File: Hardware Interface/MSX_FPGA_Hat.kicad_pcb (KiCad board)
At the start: 2 copper layers, 103 x 66 mm, 26 parts, among them J1 J1, J2 J2, J3a1 J3a, J3b1 J3b, J4a1 J4a, J4b1 J4b, U1 74LVC245A, U2 74LVC245A, U3 74LVC245A, U4 74LVC245A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

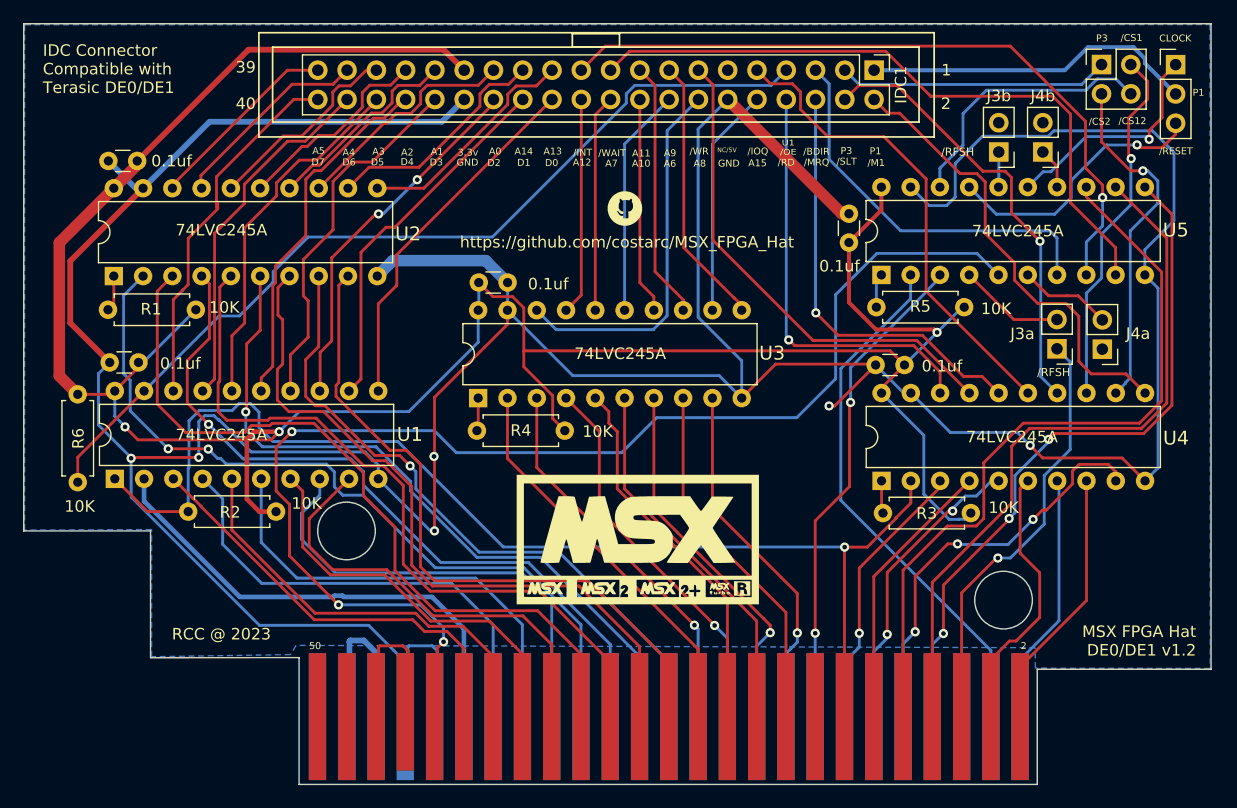
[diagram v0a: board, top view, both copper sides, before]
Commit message: Updated Add-On with silk in addresses for RPI
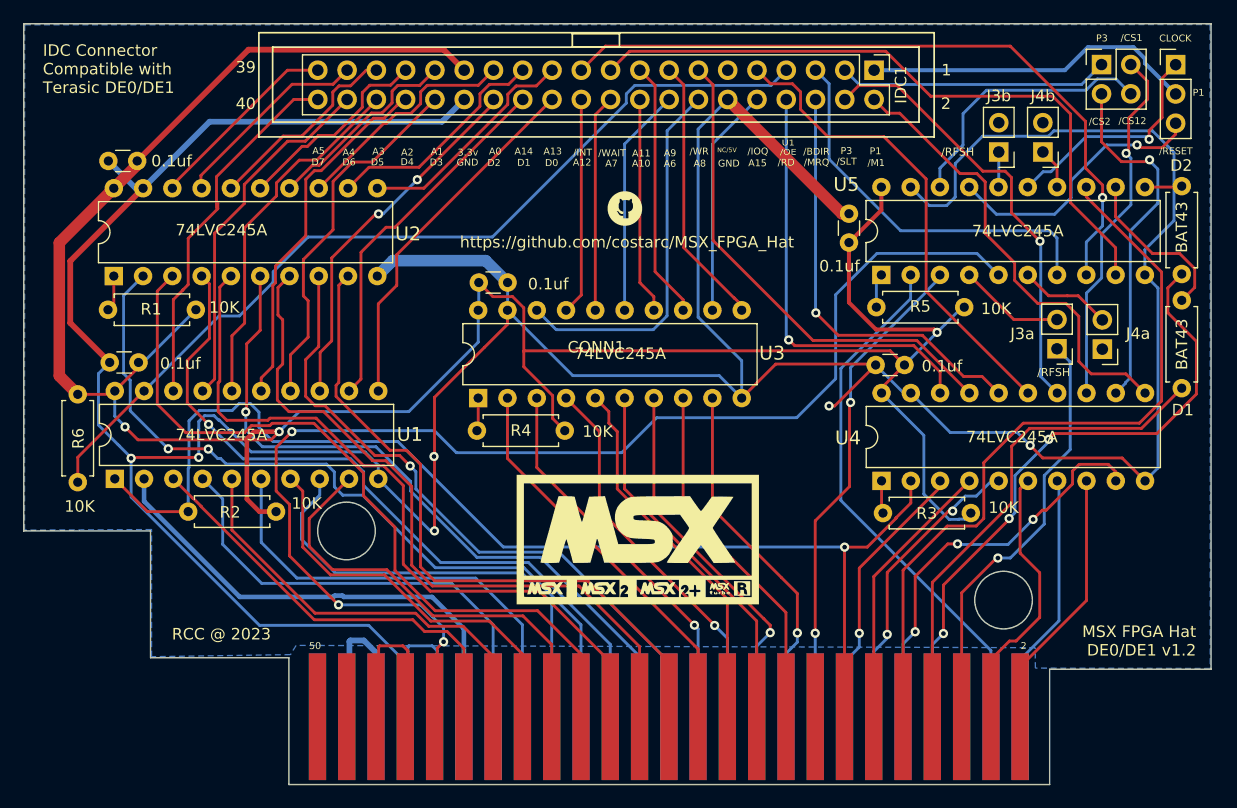
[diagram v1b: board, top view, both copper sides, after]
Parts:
- added D1: BAT43, Resistor_THT:R_Axial_DIN0207_L6.3mm_D2.5mm_P7.62mm_Horizontal, F.Cu at (152.4, 51.8)
- added D2: BAT43, Resistor_THT:R_Axial_DIN0207_L6.3mm_D2.5mm_P7.62mm_Horizontal, F.Cu at (152.4, 41.9)
- CONN1: footprint Roni Footprints:MSX_CART_SW -> Roni Footprints:MSX_CART
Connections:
- U5 pad 11: /WAIT -> Net-(U5-Pad11)
- U5 pad 12: /INT -> Net-(D1-Pad2)
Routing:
- net /INT: track 66.6 -> 47.9 mm
- net Net-(D1-Pad2): track 0.00 -> 14.5 mm
- net /WAIT: track 60.1 -> 54.6 mm
- net Net-(U5-Pad11): track 0.00 -> 3.23 mm
- net /C_CS2: track 30.4 -> 31.1 mm
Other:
- outline, holes or cut-outs redrawn

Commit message: Updated schema and pcb with some cool silk and instructions
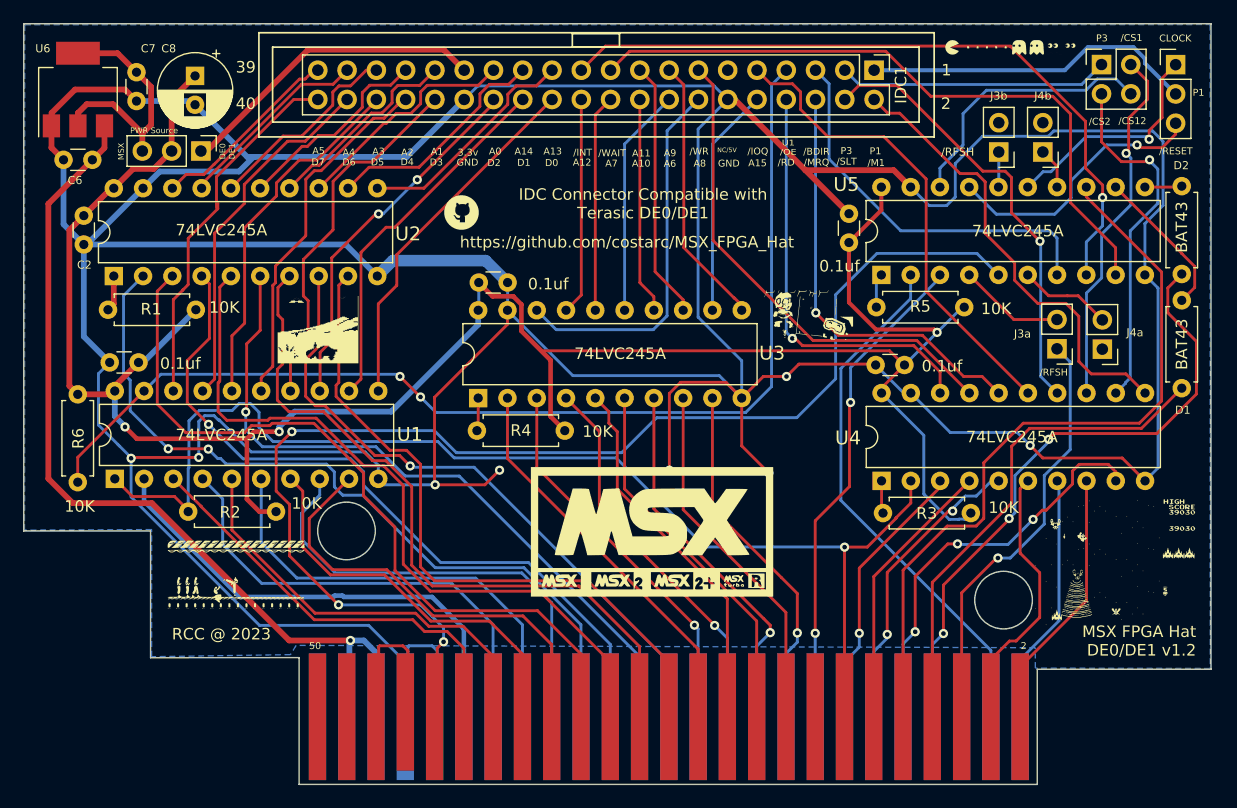
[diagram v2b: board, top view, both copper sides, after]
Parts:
- added C6: 0.1uf, Capacitor_THT:C_Disc_D3.0mm_W1.6mm_P2.50mm, F.Cu at (57.9, 32.0)
- added C7: 0.1uf, Capacitor_THT:C_Disc_D3.0mm_W1.6mm_P2.50mm, F.Cu at (61.7, 24.4)
- added C8: 100uF, Capacitor_THT:CP_Radial_D6.3mm_P2.50mm, F.Cu at (66.8, 24.7)
- added G***: LOGO, LOGO, F.Cu at (70.4, 67.8)
- added G***: LOGO, LOGO, F.Cu at (137.7, 22.9)
- added G***: LOGO, LOGO, F.Cu at (77.5, 46.7)
- added G***: LOGO, LOGO, F.Cu at (146.6, 67.1)
- added G***: LOGO, LOGO, F.Cu at (119.9, 45.5)
- added J5: Conn_01x03_Female, Connector_PinHeader_2.54mm:PinHeader_1x03_P2.54mm_Vertical, F.Cu at (67.3, 31.2)
- added U6: LM1117-3.3, Package_TO_SOT_SMD:SOT-223-3_TabPin2, F.Cu at (56.6, 25.9)
- CONN1: footprint Roni Footprints:MSX_CART -> Roni Footprints:MSX_CART_SW
- moved G*** 14.2 mm to (89.9, 36.6)
- moved C2 7.55 mm to (57.1, 39.4), turned to 90 degrees
- moved G*** 1.40 mm to (106.4, 64.3)
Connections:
- IDC1 pad 29: Vdd -> DE_3.3V
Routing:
- net GNDREF: track 359.9 -> 464.2 mm, vias 6 -> 8
- net +5V: track 15.7 -> 80.4 mm, vias 0 -> 1
- net Vdd: track 220.9 -> 192.5 mm
- net DE_3.3V: track 0.00 -> 27.2 mm
- net MSX_3.3V: track 0.00 -> 21.5 mm
- net /C_U1_D_OE: track 78.5 -> 95.6 mm, vias 0 -> 2
- net Net-(D1-Pad2): track 14.5 -> 13.1 mm
- net A14: track 57.6 -> 56.7 mm
- net C_A4: track 17.6 -> 17.1 mm
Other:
- outline, holes or cut-outs redrawn
- board text added: "DE0 DE1"
- board text added: "MSX"
- board text added: "PWR Source"

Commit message: Added pull-ups for int,wait,busdir (optional)
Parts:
- removed the G*** at (146.6, 67.1)
- added G***: LOGO, LOGO, F.Cu at (147.3, 70.4)
- added G***: LOGO, LOGO, F.Cu at (55.6, 45.7)
- added R7: 10K, Resistor_THT:R_Axial_DIN0207_L6.3mm_D2.5mm_P7.62mm_Horizontal, F.Cu at (142.1, 62.6)
- added R8: 10K, Resistor_THT:R_Axial_DIN0207_L6.3mm_D2.5mm_P7.62mm_Horizontal, F.Cu at (123.2, 52.3)
- added R9: 10K, Resistor_THT:R_Axial_DIN0207_L6.3mm_D2.5mm_P7.62mm_Horizontal, F.Cu at (152.9, 31.7)
- moved G*** 2.17 mm to (108.5, 63.5)
- moved J1 1.17 mm to (144.3, 23.7)
- moved J2 0.76 mm to (151.4, 23.2)
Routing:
- net Vdd: track 192.5 -> 268.7 mm
- net /WAIT: track 54.6 -> 71.6 mm
- net /INT: track 47.9 -> 59.8 mm
- net /BUSDIR: track 65.3 -> 67.9 mm
- net /C_CS12: track 23.5 -> 21.3 mm
- net CLOCK: track 110.0 -> 108.3 mm
- net /CS12: track 46.2 -> 47.8 mm
- net /C_CS_SLT: track 23.5 -> 22.3 mm
- net C_CLK_OR_RST: track 28.9 -> 28.1 mm
- net /C_RESET: track 23.8 -> 24.6 mm
- net /RFSH: track 37.0 -> 36.4 mm
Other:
- board text added: "MSX FPGA Hat DE0/DE1"
- board text added: "v 1.2"
- board text removed: "MSX FPGA Hat DE0/DE1 v1.2"
